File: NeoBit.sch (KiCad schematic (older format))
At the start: 13 parts, among them J2 Barrel_Jack_MountingPin, J4 NeoPixels, J5 microbit_edge_connector, U1 74AHCT125, U2 MCP1702-3302E_TO92

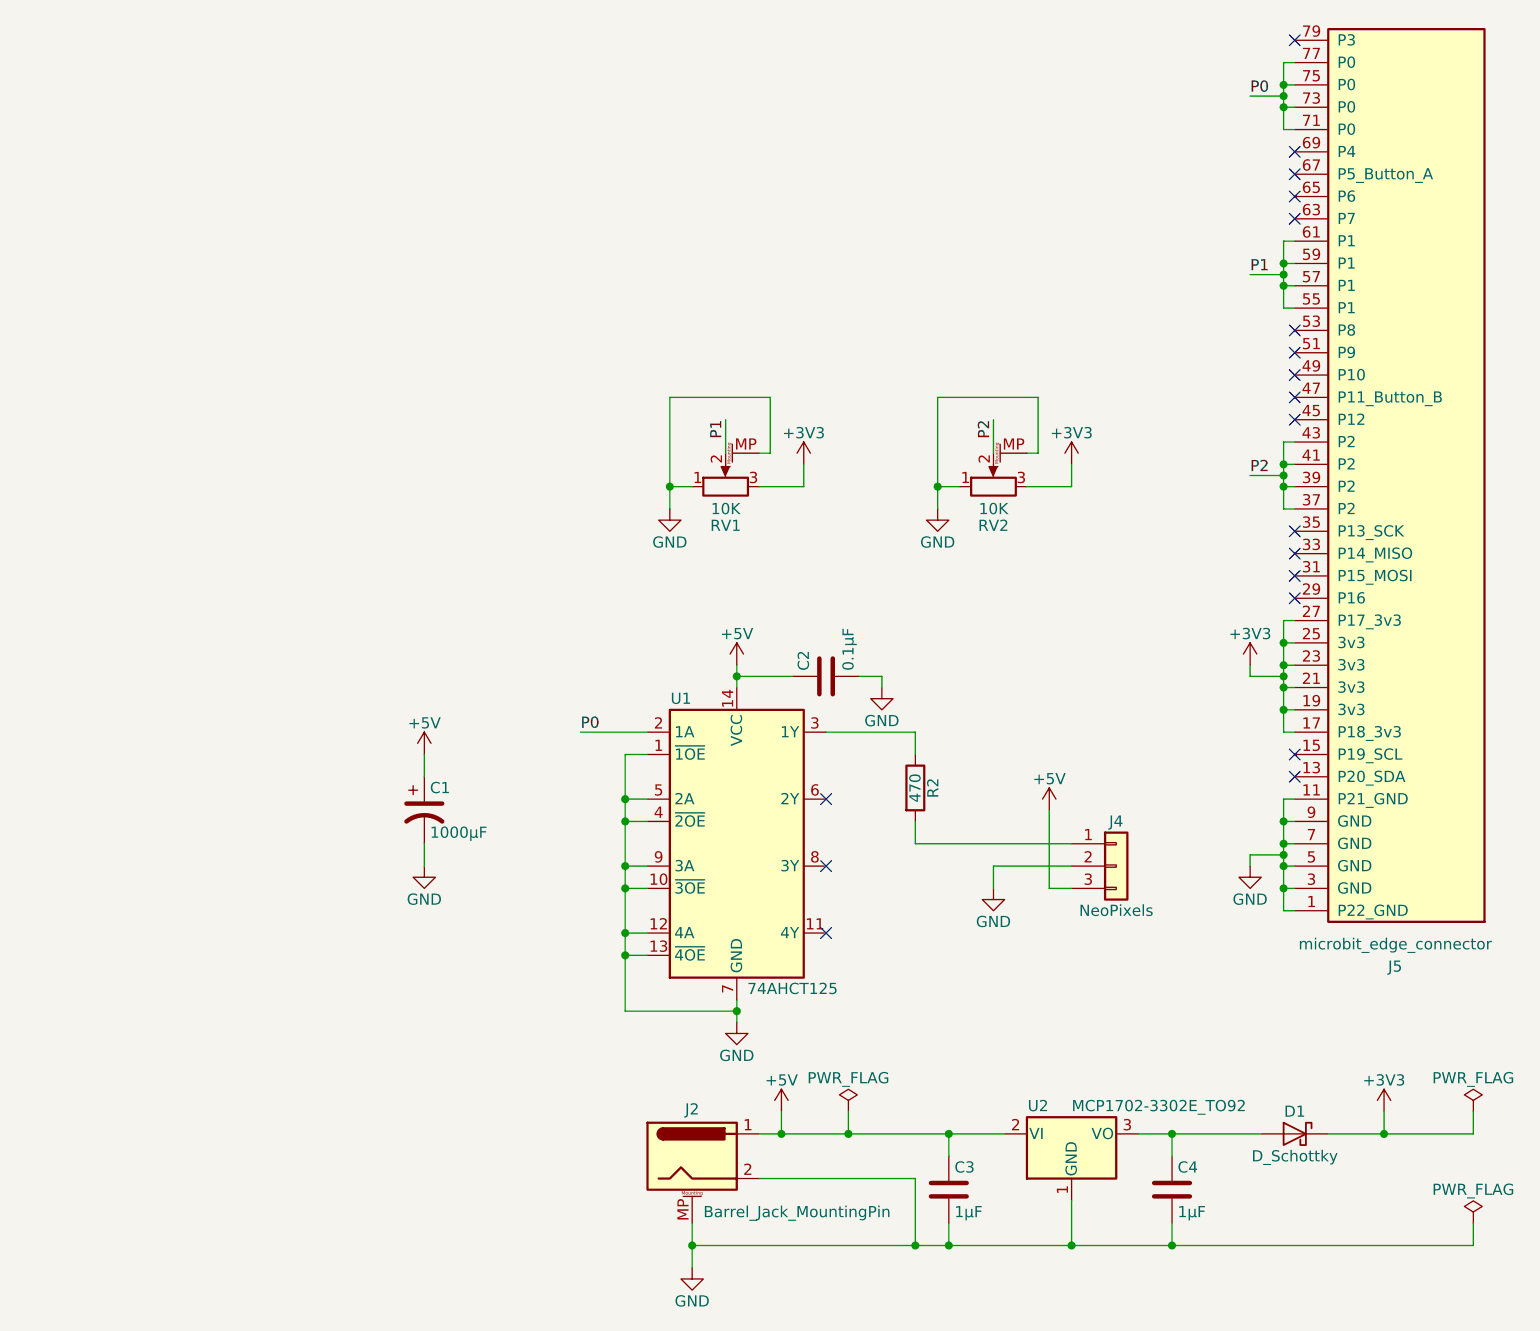
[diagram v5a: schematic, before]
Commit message: Added 5V regulator.
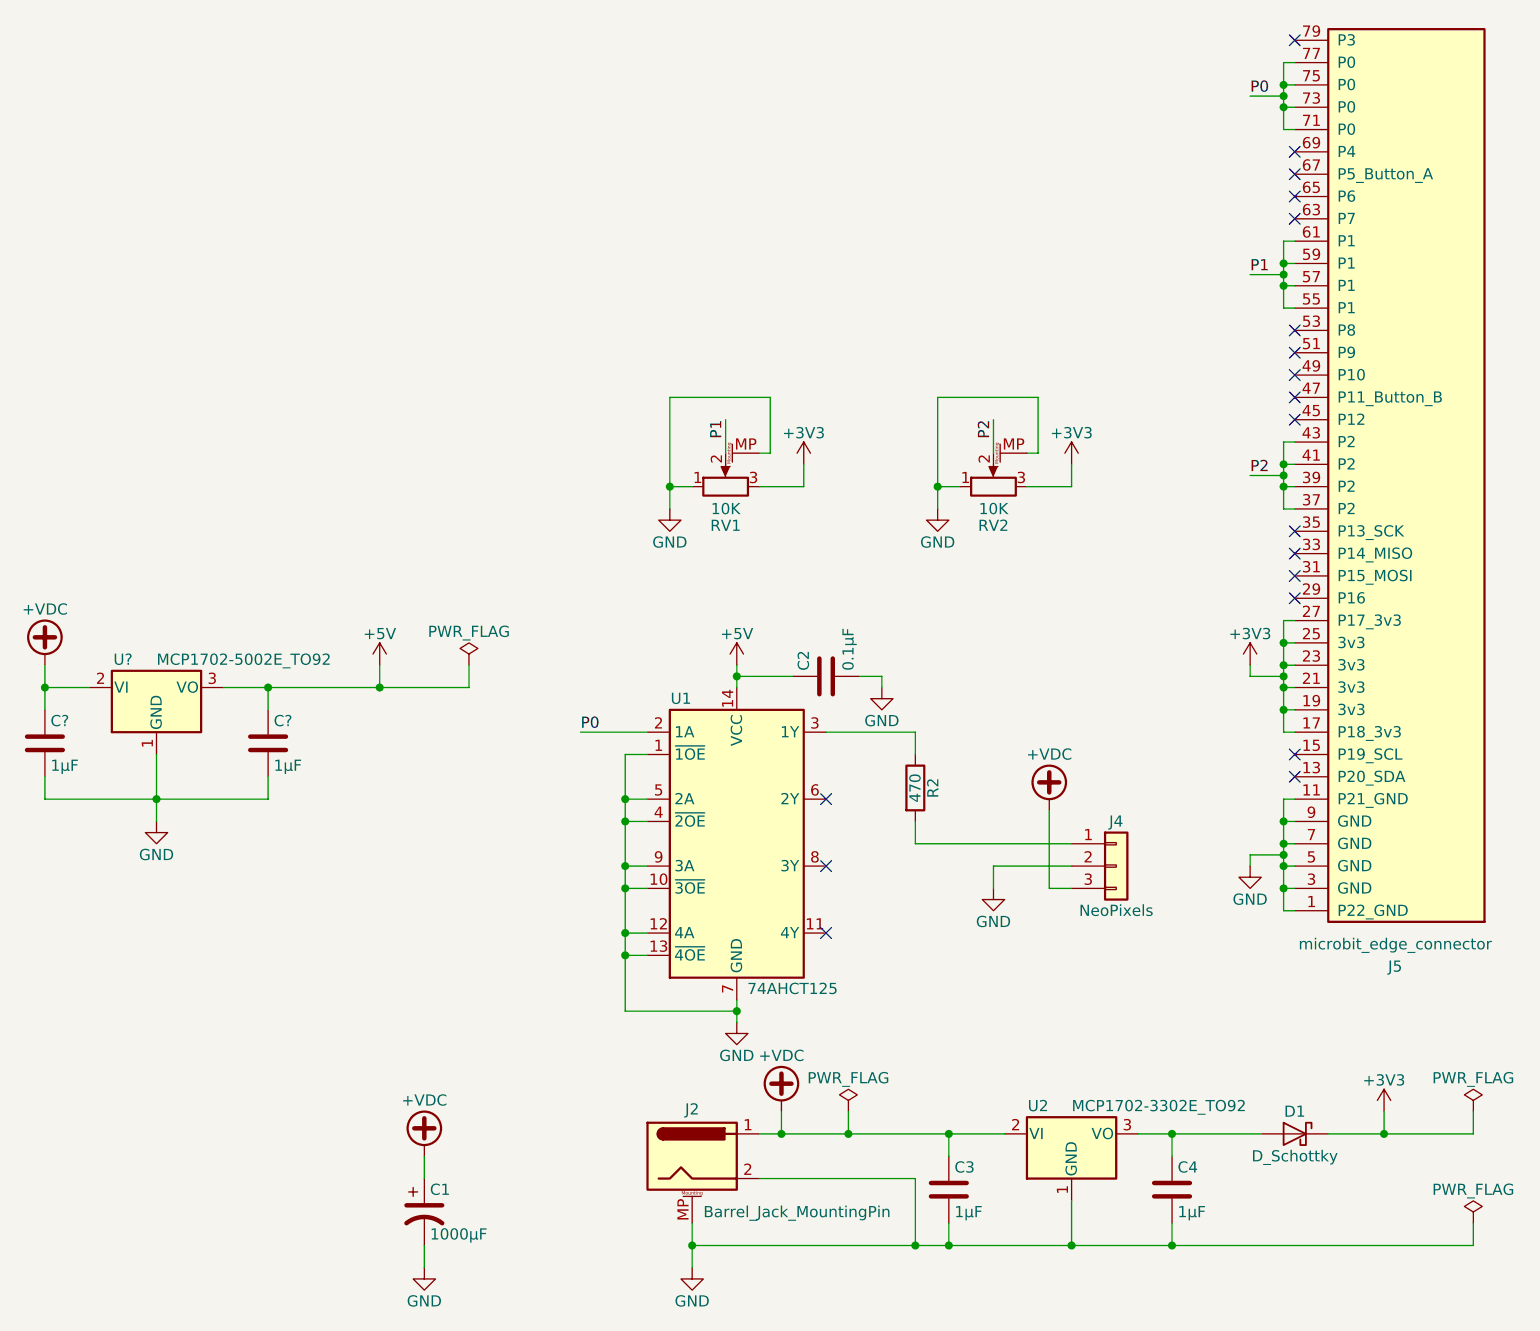
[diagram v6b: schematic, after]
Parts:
- added C? (x2): 1µF, Capacitors_THT:C_Rect_L7.0mm_W2.5mm_P5.00mm, symbol C
- added U?: MCP1702-5002E_TO92, TO_SOT_Packages_THT:TO-92_Inline_Narrow_Oval, symbol MCP1700-5002E_TO92
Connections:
- net +5V: now also C?.1, U?.3 (VO); no longer C1.1, C3.1, J2.1, J4.3 (Pin_3), U2.2 (VI)
- net GND: now also C?.2, C?.2, U?.1 (GND)
- new net +VDC: C1.1, C3.1, C?.1, J2.1, J4.3 (Pin_3), U2.2 (VI), U?.2 (VI)
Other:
- moved on the sheet: C1
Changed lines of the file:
@@
 LIBS:contrib
 LIBS:valves
-LIBS:feather
 LIBS:lib_microbit_connector
 LIBS:misc_lib
@@
 L +5V #PWR04
 U 1 1 5B8794C4
-P 6100 4650
-F 0 "#PWR04" H 6100 4500 50  0001 C CNN
-F 1 "+5V" H 6100 4790 50  0000 C CNN
-F 2 "" H 6100 4650 50  0001 C CNN
-F 3 "" H 6100 4650 50  0001 C CNN
-	1    6100 4650
+P 3100 4000
+F 0 "#PWR04" H 3100 3850 50  0001 C CNN
+F 1 "+5V" H 3100 4140 50  0000 C CNN
+F 2 "" H 3100 4000 50  0001 C CNN
+F 3 "" H 3100 4000 50  0001 C CNN
+	1    3100 4000
 	1    0    0    -1
 $EndComp
@@
 Wire Wire Line
 	4700 5500 4700 5600
-$Comp
-L +5V #PWR07
-U 1 1 5B879F10
-P 4900 6000
-F 0 "#PWR07" H 4900 5850 50  0001 C CNN
-F 1 "+5V" H 4900 6140 50  0000 C CNN
-F 2 "" H 4900 6000 50  0001 C CNN
-F 3 "" H 4900 6000 50  0001 C CNN
-	1    4900 6000
-	1    0    0    -1
-$EndComp
 $Comp
 L GND #PWR08
@@
 L CP1 C1
 U 1 1 5B87D36C
-P 3300 4650
-F 0 "C1" H 3325 4750 50  0000 L CNN
-F 1 "1000µF" H 3325 4550 50  0000 L CNN
-F 2 "Capacitors_THT:CP_Radial_D10.0mm_P5.00mm" H 3300 4650 50  0001 C CNN
-F 3 "" H 3300 4650 50  0001 C CNN
-F 4 "10WXA1000MEFCT810X9" H 3300 4650 60  0001 C CNN "MPN"
-F 5 "CAP ALUM 1000UF 20% 10V RADIAL" H 3300 4650 60  0001 C CNN "Description"
-F 6 "1189-3703-1-ND" H 3300 4650 60  0001 C CNN "Digi-Key_PN"
-	1    3300 4650
+P 3300 6450
+F 0 "C1" H 3325 6550 50  0000 L CNN
+F 1 "1000µF" H 3325 6350 50  0000 L CNN
+F 2 "Capacitors_THT:CP_Radial_D10.0mm_P5.00mm" H 3300 6450 50  0001 C CNN
+F 3 "" H 3300 6450 50  0001 C CNN
+F 4 "10WXA1000MEFCT810X9" H 3300 6450 60  0001 C CNN "MPN"
+F 5 "CAP ALUM 1000UF 20% 10V RADIAL" H 3300 6450 60  0001 C CNN "Description"
+F 6 "1189-3703-1-ND" H 3300 6450 60  0001 C CNN "Digi-Key_PN"
+	1    3300 6450
 	1    0    0    -1
 $EndComp
@@
 L GND #PWR011
 U 1 1 5B87D3B2
-P 3300 4900
-F 0 "#PWR011" H 3300 4650 50  0001 C CNN
-F 1 "GND" H 3300 4750 50  0000 C CNN
-F 2 "" H 3300 4900 50  0001 C CNN
-F 3 "" H 3300 4900 50  0001 C CNN
-	1    3300 4900
-	1    0    0    -1
-$EndComp
-$Comp
-L +5V #PWR012
-U 1 1 5B87D3F6
-P 3300 4400
-F 0 "#PWR012" H 3300 4250 50  0001 C CNN
-F 1 "+5V" H 3300 4540 50  0000 C CNN
-F 2 "" H 3300 4400 50  0001 C CNN
-F 3 "" H 3300 4400 50  0001 C CNN
-	1    3300 4400
-	1    0    0    -1
-$EndComp
-Wire Wire Line
-	3300 4500 3300 4400
-Wire Wire Line
-	3300 4800 3300 4900
+P 3300 6700
+F 0 "#PWR011" H 3300 6450 50  0001 C CNN
+F 1 "GND" H 3300 6550 50  0000 C CNN
+F 2 "" H 3300 6700 50  0001 C CNN
+F 3 "" H 3300 6700 50  0001 C CNN
+	1    3300 6700
+	1    0    0    -1
+$EndComp
+Wire Wire Line
+	3300 6300 3300 6200
+Wire Wire Line
+	3300 6600 3300 6700
 $Comp
 L PWR_FLAG #FLG013
@@
 Wire Wire Line
 	7600 6000 7600 6100
+$Comp
+L +VDC #PWR?
+U 1 1 5BA32D90
+P 3300 6200
+F 0 "#PWR?" H 3300 6100 50  0001 C CNN
+F 1 "+VDC" H 3300 6450 50  0000 C CNN
+F 2 "" H 3300 6200 50  0001 C CNN
+F 3 "" H 3300 6200 50  0001 C CNN
+	1    3300 6200
+	1    0    0    -1
+$EndComp
+$Comp
+L +VDC #PWR?
+U 1 1 5BA32FD2
+P 6100 4650
+F 0 "#PWR?" H 6100 4550 50  0001 C CNN
+F 1 "+VDC" H 6100 4900 50  0000 C CNN
+F 2 "" H 6100 4650 50  0001 C CNN
+F 3 "" H 6100 4650 50  0001 C CNN
+	1    6100 4650
+	1    0    0    -1
+$EndComp
+$Comp
+L +VDC #PWR?
+U 1 1 5BA33004
+P 4900 6000
+F 0 "#PWR?" H 4900 5900 50  0001 C CNN
+F 1 "+VDC" H 4900 6250 50  0000 C CNN
+F 2 "" H 4900 6000 50  0001 C CNN
+F 3 "" H 4900 6000 50  0001 C CNN
+	1    4900 6000
+	1    0    0    -1
+$EndComp
+$Comp
+L MCP1700-5002E_TO92 U?
+U 1 1 5BA331CB
+P 2100 4100
+F 0 "U?" H 1950 3975 50  0000 C CNN
+F 1 "MCP1702-5002E_TO92" H 2100 3975 50  0000 L CNN
+F 2 "TO_SOT_Packages_THT:TO-92_Inline_Narrow_Oval" H 2100 3900 50  0001 C CIN
+F 3 "" H 2100 4100 50  0001 C CNN
+	1    2100 4100
+	1    0    0    1
+$EndComp
+$Comp
+L C C?
+U 1 1 5BA3332C
+P 1600 4350
+F 0 "C?" H 1625 4450 50  0000 L CNN
+F 1 "1µF" H 1625 4250 50  0000 L CNN
+F 2 "Capacitors_THT:C_Rect_L7.0mm_W2.5mm_P5.00mm" H 1638 4200 50  0001 C CNN
+F 3 "" H 1600 4350 50  0001 C CNN
+F 4 "K105Z20Y5VF5TH5" H 1600 4350 60  0001 C CNN "MPN"
+F 5 "CAP CER 1UF 50V Y5V RADIAL" H 1600 4350 60  0001 C CNN "Description"
+F 6 "BC1168CT-ND" H 1600 4350 60  0001 C CNN "Digi-Key_PN"
+	1    1600 4350
+	1    0    0    -1
+$EndComp
+$Comp
+L C C?
+U 1 1 5BA3337C
+P 2600 4350
+F 0 "C?" H 2625 4450 50  0000 L CNN
+F 1 "1µF" H 2625 4250 50  0000 L CNN
+F 2 "Capacitors_THT:C_Rect_L7.0mm_W2.5mm_P5.00mm" H 2638 4200 50  0001 C CNN
+F 3 "" H 2600 4350 50  0001 C CNN
+F 4 "K105Z20Y5VF5TH5" H 2600 4350 60  0001 C CNN "MPN"
+F 5 "CAP CER 1UF 50V Y5V RADIAL" H 2600 4350 60  0001 C CNN "Description"
+F 6 "BC1168CT-ND" H 2600 4350 60  0001 C CNN "Digi-Key_PN"
+	1    2600 4350
+	1    0    0    -1
+$EndComp
+$Comp
+L +VDC #PWR?
+U 1 1 5BA3347F
+P 1600 4000
+F 0 "#PWR?" H 1600 3900 50  0001 C CNN
+F 1 "+VDC" H 1600 4250 50  0000 C CNN
+F 2 "" H 1600 4000 50  0001 C CNN
+F 3 "" H 1600 4000 50  0001 C CNN
+	1    1600 4000
+	1    0    0    -1
+$EndComp
+$Comp
+L GND #PWR?
+U 1 1 5BA33626
+P 2100 4700
+F 0 "#PWR?" H 2100 4450 50  0001 C CNN
+F 1 "GND" H 2100 4550 50  0000 C CNN
+F 2 "" H 2100 4700 50  0001 C CNN
+F 3 "" H 2100 4700 50  0001 C CNN
+	1    2100 4700
+	1    0    0    -1
+$EndComp
+Wire Wire Line
+	1600 4000 1600 4200
+Wire Wire Line
+	1800 4100 1600 4100
+Connection ~ 1600 4100
+Wire Wire Line
+	2400 4100 3500 4100
+Wire Wire Line
+	3100 4100 3100 4000
+Wire Wire Line
+	2600 4200 2600 4100
+Connection ~ 2600 4100
+Wire Wire Line
+	1600 4500 1600 4600
+Wire Wire Line
+	1600 4600 2600 4600
+Wire Wire Line
+	2600 4600 2600 4500
+Wire Wire Line
+	2100 4400 2100 4700
+Connection ~ 2100 4600
+$Comp
+L PWR_FLAG #FLG?
+U 1 1 5BA33AB3
+P 3500 4000
+F 0 "#FLG?" H 3500 4075 50  0001 C CNN
+F 1 "PWR_FLAG" H 3500 4150 50  0000 C CNN
+F 2 "" H 3500 4000 50  0001 C CNN
+F 3 "" H 3500 4000 50  0001 C CNN
+	1    3500 4000
+	1    0    0    -1
+$EndComp
+Wire Wire Line
+	3500 4100 3500 4000
+Connection ~ 3100 4100
 $EndSCHEMATC

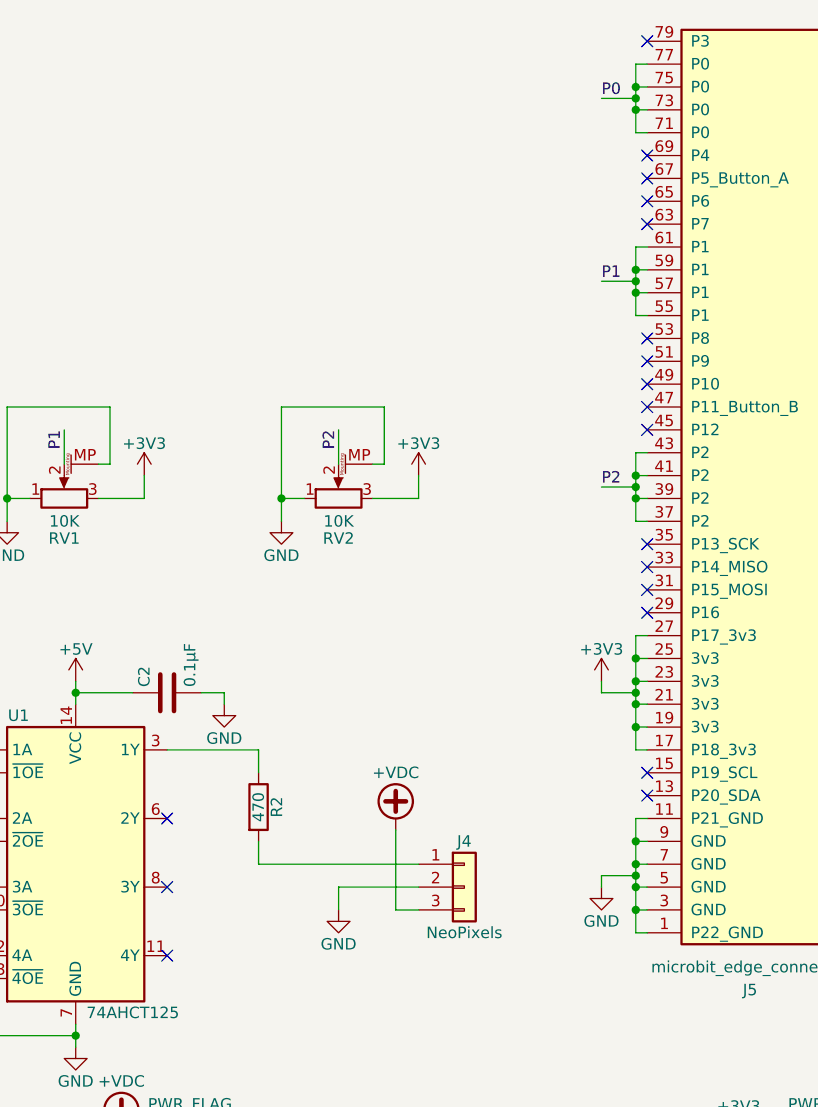
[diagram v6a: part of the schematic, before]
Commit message: Screw terminals for NeoPixels and DotStars.
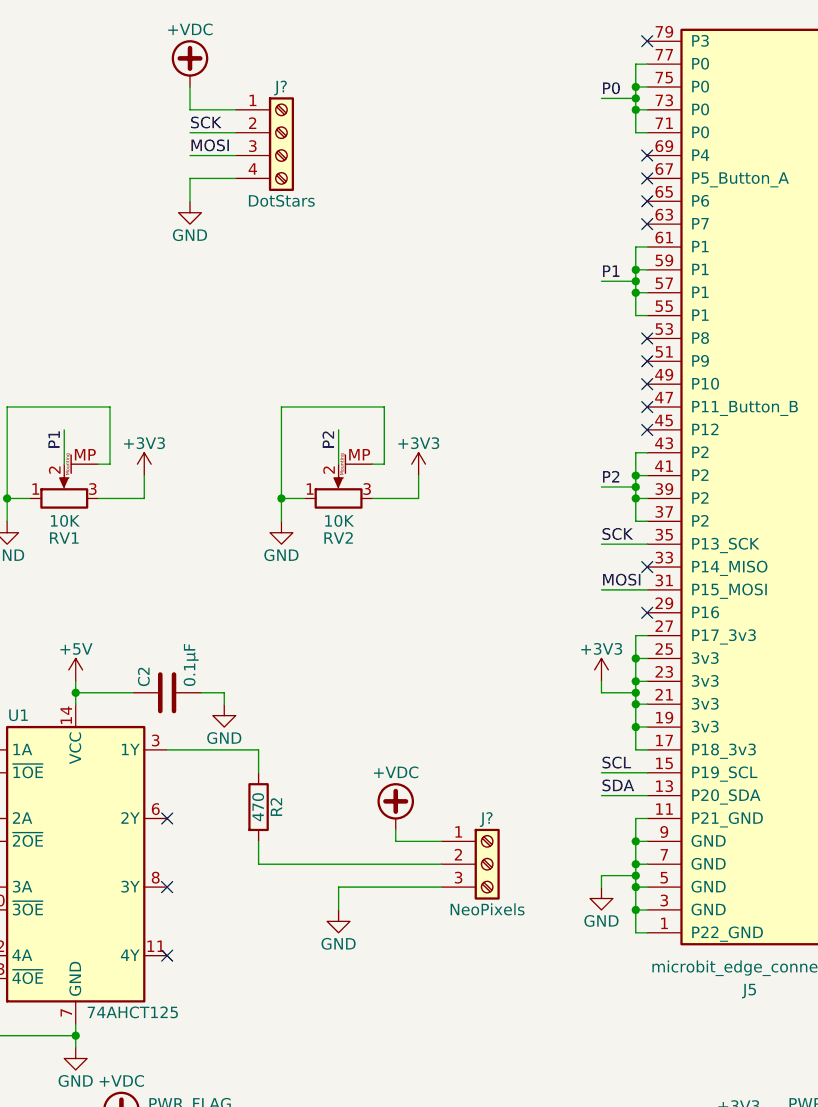
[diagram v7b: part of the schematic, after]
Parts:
- removed J4: NeoPixels, Connectors_JST:JST_PH_S3B-PH-K_03x2.00mm_Angled, symbol Conn_01x03
- added J?: NeoPixels, symbol Screw_Terminal_01x03
- added J?: DotStars, symbol Screw_Terminal_01x04
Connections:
- net +VDC: now also J?.1 (Pin_1), J?.1 (Pin_1)
- net GND: now also J?.3 (Pin_3), J?.4 (Pin_4)
- net SDA: now reaches J5.13 (P20_SDA)
- net SCL: now reaches J5.15 (P19_SCL)
- net MOSI: now reaches J5.31 (P15_MOSI)
- net MOSI: now also J?.3 (Pin_3)
- net SCK: now reaches J5.35 (P13_SCK)
- net SCK: now also J?.2 (Pin_2)
- net at R2.2: now also J?.2 (Pin_2)
- no-connect marks 19 -> 15
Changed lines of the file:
@@
 Connection ~ 7150 4850
-$Comp
-L Conn_01x03 J4
-U 1 1 5B8792D8
-P 6400 4900
-F 0 "J4" H 6400 5100 50  0000 C CNN
-F 1 "NeoPixels" H 6400 4700 50  0000 C CNN
-F 2 "Connectors_JST:JST_PH_S3B-PH-K_03x2.00mm_Angled" H 6400 4900 50  0001 C CNN
-F 3 "" H 6400 4900 50  0001 C CNN
-F 4 "S3B-PH-K-S(LF)(SN)" H 6400 4900 60  0001 C CNN "MPN"
-F 5 "CONN HEADER PH SIDE 3POS 2MM" H 6400 4900 60  0001 C CNN "Description"
-F 6 "455-1720-ND" H 6400 4900 60  0001 C CNN "Digi-Key_PN"
-	1    6400 4900
-	1    0    0    -1
-$EndComp
 $Comp
 L GND #PWR03
@@
 Wire Wire Line
 	5850 5000 5850 4900
-Wire Wire Line
-	5850 4900 6200 4900
 $Comp
 L 74AHCT125 U1
@@
 Wire Wire Line
 	5100 4300 5500 4300
-Wire Wire Line
-	5500 4800 6200 4800
 Wire Wire Line
 	4300 4400 4200 4400
@@
 	1    0    0    -1
 $EndComp
-Wire Wire Line
-	6100 4650 6100 5000
-Wire Wire Line
-	6100 5000 6200 5000
 $Comp
 L R_POT_MountingPin RV1
@@
 NoConn ~ 7200 2800
 NoConn ~ 7200 2900
-NoConn ~ 7200 3400
 NoConn ~ 7200 3500
-NoConn ~ 7200 3600
 NoConn ~ 7200 3700
-NoConn ~ 7200 4400
-NoConn ~ 7200 4500
 Wire Wire Line
 	7600 6000 7600 6100
@@
 	3500 4100 3500 4000
 Connection ~ 3100 4100
+$Comp
+L Screw_Terminal_01x03 J?
+U 1 1 5BA3E89A
+P 6500 4800
+F 0 "J?" H 6500 5000 50  0000 C CNN
+F 1 "NeoPixels" H 6500 4600 50  0000 C CNN
+F 2 "" H 6500 4800 50  0001 C CNN
+F 3 "" H 6500 4800 50  0001 C CNN
+	1    6500 4800
+	1    0    0    -1
+$EndComp
+Wire Wire Line
+	6100 4650 6100 4700
+Wire Wire Line
+	6100 4700 6300 4700
+Wire Wire Line
+	5500 4800 6300 4800
+Wire Wire Line
+	5850 4900 6300 4900
+Text Label 7000 3400 0    50   ~ 0
+SCK
+Text Label 7000 3600 0    50   ~ 0
+MOSI
+Wire Wire Line
+	7000 3400 7200 3400
+Wire Wire Line
+	7000 3600 7200 3600
+Text Label 7000 4400 0    50   ~ 0
+SCL
+Text Label 7000 4500 0    50   ~ 0
+SDA
+Wire Wire Line
+	7000 4400 7200 4400
+Wire Wire Line
+	7000 4500 7200 4500
+$Comp
+L Screw_Terminal_01x04 J?
+U 1 1 5BA3F768
+P 5600 1600
+F 0 "J?" H 5600 1800 50  0000 C CNN
+F 1 "DotStars" H 5600 1300 50  0000 C CNN
+F 2 "" H 5600 1600 50  0001 C CNN
+F 3 "" H 5600 1600 50  0001 C CNN
+	1    5600 1600
+	1    0    0    -1
+$EndComp
+$Comp
+L +VDC #PWR?
+U 1 1 5BA4005E
+P 5200 1400
+F 0 "#PWR?" H 5200 1300 50  0001 C CNN
+F 1 "+VDC" H 5200 1650 50  0000 C CNN
+F 2 "" H 5200 1400 50  0001 C CNN
+F 3 "" H 5200 1400 50  0001 C CNN
+	1    5200 1400
+	1    0    0    -1
+$EndComp
+$Comp
+L GND #PWR?
+U 1 1 5BA4009C
+P 5200 1900
+F 0 "#PWR?" H 5200 1650 50  0001 C CNN
+F 1 "GND" H 5200 1750 50  0000 C CNN
+F 2 "" H 5200 1900 50  0001 C CNN
+F 3 "" H 5200 1900 50  0001 C CNN
+	1    5200 1900
+	1    0    0    -1
+$EndComp
+Text Label 5200 1600 0    50   ~ 0
+SCK
+Text Label 5200 1700 0    50   ~ 0
+MOSI
+Wire Wire Line
+	5200 1400 5200 1500
+Wire Wire Line
+	5200 1500 5400 1500
+Wire Wire Line
+	5200 1900 5200 1800
+Wire Wire Line
+	5200 1800 5400 1800
+Wire Wire Line
+	5200 1600 5400 1600
+Wire Wire Line
+	5200 1700 5400 1700
 $EndSCHEMATC
